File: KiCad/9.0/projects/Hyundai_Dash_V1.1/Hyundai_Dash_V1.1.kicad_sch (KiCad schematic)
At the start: 30 parts, among them J1 +12V-GND, J10 GND-Fuel, J2 IGN-LSG-RSG-LS1-LS2, J3 C-CAN, J4 C-CAN, J5 C-CAN SPI, J6 B-CAN, J7 B-CAN, J8 B-CAN SPI, J9 Jumper Holder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

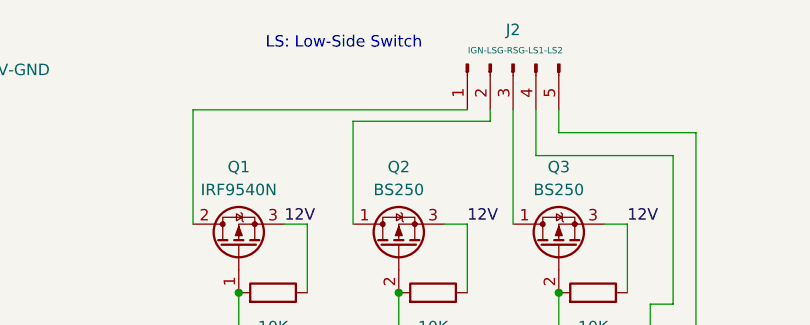
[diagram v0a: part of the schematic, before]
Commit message: KiCad: bump Hyundai Dash to v1.1
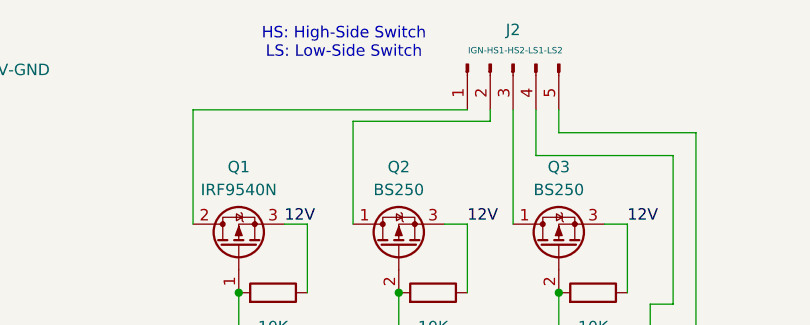
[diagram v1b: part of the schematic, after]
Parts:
- J2: value IGN-LSG-RSG-LS1-LS2 -> IGN-HS1-HS2-LS1-LS2
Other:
- note added: "HS: High-Side Switch LS: Low-Side Switch"
- note removed: "LS: Low-Side Switch"
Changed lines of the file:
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@@
 		(rev "V3")
 	)
-	(text "LS: Low-Side Switch"
+	(text "HS: High-Side Switch\nLS: Low-Side Switch"
 		(exclude_from_sim no)
 		(at 72.644 19.304 0)
@@
 			)
 		)
-		(property "Value" "IGN-LSG-RSG-LS1-LS2"
+		(property "Value" "IGN-HS1-HS2-LS1-LS2"
 			(at 91.694 20.066 90)
 			(effects
